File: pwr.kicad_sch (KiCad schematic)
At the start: 2 parts, among them J2 ATX-24, J3 Conn_02x02_Top_Bottom

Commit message: Cleanup & Debug I/O
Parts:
- removed J3: Conn_02x02_Top_Bottom, symbol Connector_Generic:Conn_02x02_Top_Bottom
- added U11: NCP1117-1.8_SOT223, Package_TO_SOT_SMD:SOT-223-3_TabPin2, symbol Regulator_Linear:NCP1117-1.8_SOT223
- added U13: NCP1117-1.5_SOT223, Package_TO_SOT_SMD:SOT-223-3_TabPin2, symbol Regulator_Linear:NCP1117-1.5_SOT223
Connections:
- net -12V: now reaches J2.14 (-12V)
- net PWR_EN: now reaches J2.16 (PS_ON#)
- net ATX_PWRGD: now reaches J2.8 (PWR_OK)
- no-connect marks 1 -> 0
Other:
- note added: "Additional Power Rails: - 1.2V - 1.8V Standby: - 1.2V_{SB} - 3.3V_{SB} - 5V_{DUAL}"
- note added: "XCGPU Power Rails: - V_CPUCORE (0.9V - 1.2V) - V_CPUEDRAM (1.075V) - V_MEM (1.8V) - V_CPUVCS (1.25V - 1.3V) Low Power: - V_GPUPCIE (1.5V) - V_EFUSE (1.5V)"

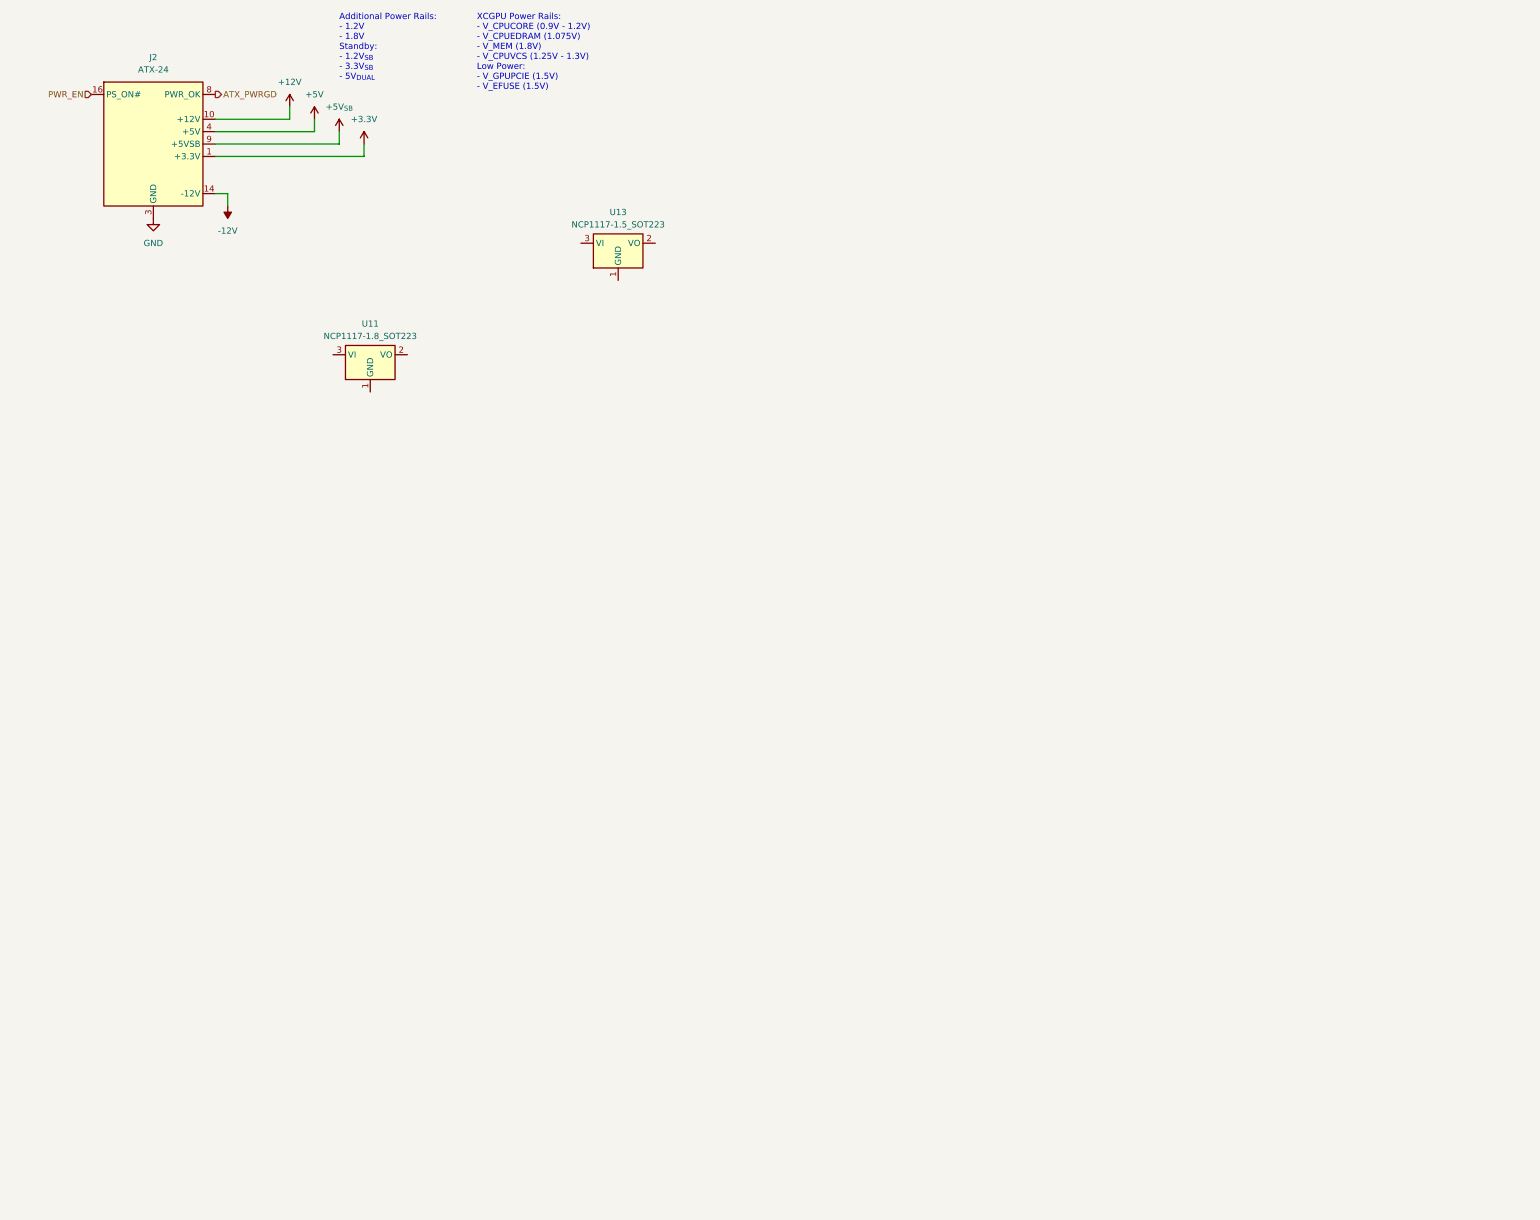
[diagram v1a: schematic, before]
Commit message: Multipurpose and standby power rails, Reannotated schematic
Added V_1P2, V_1P8, V_5P0DUAL, V_EFUSE, V_GPUPCIE, V_3P3STBY and V_1P2STBY
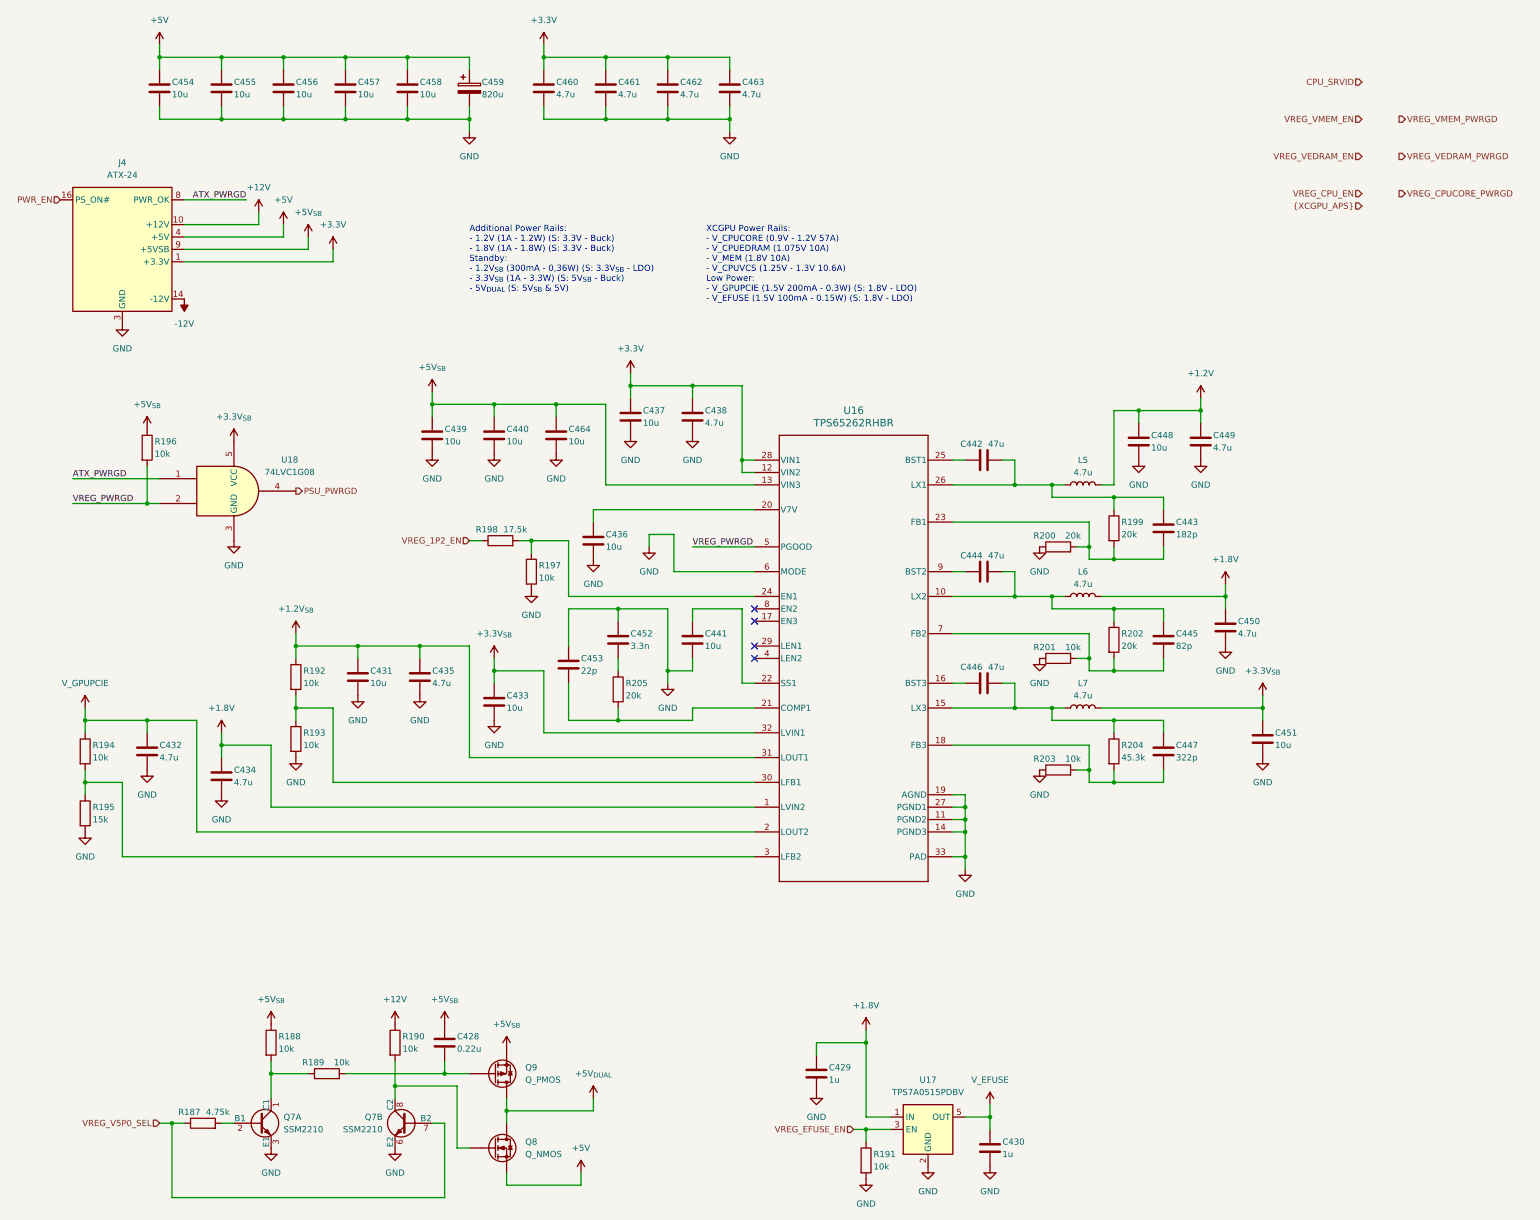
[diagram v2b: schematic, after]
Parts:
- removed U11: NCP1117-1.8_SOT223, Package_TO_SOT_SMD:SOT-223-3_TabPin2, symbol Regulator_Linear:NCP1117-1.8_SOT223
- removed U13: NCP1117-1.5_SOT223, Package_TO_SOT_SMD:SOT-223-3_TabPin2, symbol Regulator_Linear:NCP1117-1.5_SOT223
- added C428: 0.22u, symbol Device:C
- added C429, C430: 1u, symbol Device:C
- added C431, C433, C436, C437, C439, C440, C441, C448, C451, C454, C455, C456, C457, C458, C464: 10u, symbol Device:C
- added C432, C434, C435, C438, C449, C450, C460, C461, C462, C463: 4.7u, symbol Device:C
- added C442, C444, C446: 47u, symbol Device:C
- added C443: 182p, symbol Device:C
- added C445: 82p, symbol Device:C
- added C447: 322p, symbol Device:C
- added C452: 3.3n, symbol Device:C
- added C453: 22p, symbol Device:C
- added C459: 820u, symbol Device:C_Polarized
- added L5, L6, L7: 4.7u, symbol Device:L
- added Q7: SSM2210, symbol Transistor_BJT:SSM2210
- added Q8: Q_NMOS, symbol Device:Q_NMOS
- added Q9: Q_PMOS, symbol Device:Q_PMOS
- added R187: 4.75k, symbol Device:R
- added R188, R189, R190, R191, R192, R193, R194, R196, R197, R201, R203: 10k, symbol Device:R
- added R195: 15k, symbol Device:R
- added R198: 17.5k, symbol Device:R
- added R199, R200, R202, R205: 20k, symbol Device:R
- added R204: 45.3k, symbol Device:R
- added U16: TPS65262RHBR, RHB0032E, symbol TPS65262:TPS65262RHBR
- added U17: TPS7A0515PDBV, Package_TO_SOT_SMD:SOT-23-5, symbol Regulator_Linear:TPS7A0515PDBV
- added U18: 74LVC1G08, symbol 74xGxx:74LVC1G08
- renumbered J2 to J4
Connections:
- net +12V: now also R190.1
- net +3.3V: now also C437.1, C438.1, C460.1, C461.1, C462.1, C463.1, U16.12 (VIN2), U16.28 (VIN1)
- net +5V: now also C454.1, C455.1, C456.1, C457.1, C458.1, C459.1, Q8.S
- net +5V_{SB}: now also C428.1, C439.1, C440.1, C464.1, Q9.S, R188.1, R196.1, U16.13 (VIN3)
- net ATX_PWRGD: now also U18.1
- net GND: now also C429.2, C430.2, C431.2, C432.2, C433.2, C434.2, C435.2, C436.2, C437.2, C438.2, C439.2, C440.2, C441.2, C448.2, C449.2, C450.2, C451.2, C452.1, C453.1, C454.2, C455.2, C456.2, C457.2, C458.2, C459.2, C460.2, C461.2, C462.2, C463.2, C464.2, Q7.3 (E1), Q7.6 (E2), R191.2, R193.2, R195.2, R197.2, R200.1, R201.1, R203.1, U16.11 (PGND2), U16.14 (PGND3), U16.19 (AGND), U16.27 (PGND1), U16.33 (PAD), U16.6 (MODE), U17.2 (GND), U18.3 (GND)
- new net: Q7.8 (C2), Q8.G, R190.2
- new net: Q7.2 (B1), R187.2
- new net: C453.2, R205.2, U16.21 (COMP1)
- new net: R197.1, R198.2, U16.24 (EN1)
- new net: C442.2, C443.1, L5.1, R199.1, U16.26 (LX1)
- new net: Q7.1 (C1), R188.2, R189.1
- new net: C428.2, Q9.G, R189.2
- new net: C443.2, R199.2, R200.2, U16.23 (FB1)
- new net: C445.2, R201.2, R202.2, U16.7 (FB2)
- new net: C444.2, C445.1, L6.1, R202.1, U16.10 (LX2)
- new net: C452.2, R205.1
- new net: C442.1, U16.25 (BST1)
- new net: C446.2, C447.1, L7.1, R204.1, U16.15 (LX3)
- new net: C447.2, R203.2, R204.2, U16.18 (FB3)
- new net: C444.1, U16.9 (BST2)
- new net: R194.2, R195.1, U16.3 (LFB2)
- new net: R192.2, R193.1, U16.30 (LFB1)
- new net: C436.1, U16.20 (V7V)
- new net: C441.1, U16.22 (SS1)
- new net: C446.1, U16.16 (BST3)
- new net +1.2V: C448.1, C449.1, L5.2
- new net +1.2V_{SB}: C431.1, C435.1, R192.1, U16.31 (LOUT1)
- new net +1.8V: C429.1, C434.1, C450.1, L6.2, U16.1 (LVIN2), U17.1 (IN)
- new net +3.3V_{SB}: C433.1, C451.1, L7.2, U16.32 (LVIN1), U18.5 (VCC)
- new net +5V_{DUAL}: Q8.D, Q9.D
- new net PSU_PWRGD: U18.4
- new net VREG_1P2_EN: R198.1
- new net VREG_EFUSE_EN: R191.1, U17.3 (EN)
- new net VREG_PWRGD: R196.2, U16.5 (PGOOD), U18.2
- new net VREG_V5P0_SEL: Q7.7 (B2), R187.1
- new net V_EFUSE: C430.1, U17.5 (OUT)
- new net V_GPUPCIE: C432.1, R194.1, U16.2 (LOUT2)
- no-connect marks 0 -> 4
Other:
- note added: "Additional Power Rails: - 1.2V (1A - 1.2W) (S: 3.3V - Buck) - 1.8V (1A - 1.8W) (S: 3.3V - Buck) Standby: - 1.2V_{SB} (300mA - 0,36W) (S: 3.3V_{SB} - LDO) - 3.3V_{SB} (1A - 3.3W) (S: 5V_{SB} - Buck) - 5V_{DUAL} (S: 5V_{SB} & 5V)"
- note added: "XCGPU Power Rails: - V_CPUCORE (0.9V - 1.2V 57A) - V_CPUEDRAM (1.075V 10A) - V_MEM (1.8V 10A) - V_CPUVCS (1.25V - 1.3V 10.6A) Low Power: - V_GPUPCIE (1.5V 200mA - 0.3W) (S: 1.8V - LDO) - V_EFUSE (1.5V 100mA - 0.15W) (S: 1.8V - LDO)"
- note removed: "Additional Power Rails: - 1.2V - 1.8V Standby: - 1.2V_{SB} - 3.3V_{SB} - 5V_{DUAL}"
- note removed: "XCGPU Power Rails: - V_CPUCORE (0.9V - 1.2V) - V_CPUEDRAM (1.075V) - V_MEM (1.8V) - V_CPUVCS (1.25V - 1.3V) Low Power: - V_GPUPCIE (1.5V) - V_EFUSE (1.5V)"
- moved on the sheet: J4
